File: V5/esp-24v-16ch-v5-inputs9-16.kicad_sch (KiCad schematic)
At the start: 10 parts, among them U11 OR-3H7-4

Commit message: Created V5
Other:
- title: ESP 24V 16xIn/16xOut/4xNTC Module -> ESP 24V 16xIn/16xOut/1-Wire Module
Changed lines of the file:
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@@
 	(paper "A4")
 	(title_block
-		(title "ESP 24V 16xIn/16xOut/4xNTC Module")
-		(date "2025-07-04")
-		(rev "V4.1")
+		(title "ESP 24V 16xIn/16xOut/1-Wire Module")
+		(date "2025-12-09")
+		(rev "V5")
 	)
 	(text "I_{LED} = (24V - V_{LED}) / 6.8k\nI_{LED} = (24V - 2.7V) / 6.8k\nI_{LED} = 3,13 mA"
@@
 		)
 		(instances
-			(project "esp-24v-16ch-v4"
+			(project "esp-24v-16ch-v5"
 				(path "/2bc5a21a-1d79-419d-a592-6852cc07b00a/33bd2dd9-fdba-4639-85e9-44cc18eb8635"
 					(reference "R71")
@@
 		)
 		(instances
-			(project "esp-24v-16ch-v4"
+			(project "esp-24v-16ch-v5"
 				(path "/2bc5a21a-1d79-419d-a592-6852cc07b00a/33bd2dd9-fdba-4639-85e9-44cc18eb8635"
 					(reference "#PWR073")
@@
 		)
 		(instances
-			(project "esp-24v-16ch-v4"
+			(project "esp-24v-16ch-v5"
 				(path "/2bc5a21a-1d79-419d-a592-6852cc07b00a/33bd2dd9-fdba-4639-85e9-44cc18eb8635"
 					(reference "#PWR071")
@@
 		)
 		(instances
-			(project "esp-24v-16ch-v4"
+			(project "esp-24v-16ch-v5"
 				(path "/2bc5a21a-1d79-419d-a592-6852cc07b00a/33bd2dd9-fdba-4639-85e9-44cc18eb8635"
 					(reference "FB11")
@@
 		)
 		(instances
-			(project "esp-24v-16ch-v4"
+			(project "esp-24v-16ch-v5"
 				(path "/2bc5a21a-1d79-419d-a592-6852cc07b00a/33bd2dd9-fdba-4639-85e9-44cc18eb8635"
 					(reference "D39")
@@
 		)
 		(instances
-			(project "esp-24v-16ch-v4"
+			(project "esp-24v-16ch-v5"
 				(path "/2bc5a21a-1d79-419d-a592-6852cc07b00a/33bd2dd9-fdba-4639-85e9-44cc18eb8635"
 					(reference "C51")
@@
 		)
 		(instances
-			(project "esp-24v-16ch-v4"
+			(project "esp-24v-16ch-v5"
 				(path "/2bc5a21a-1d79-419d-a592-6852cc07b00a/33bd2dd9-fdba-4639-85e9-44cc18eb8635"
 					(reference "#PWR075")
@@
 		)
 		(instances
-			(project "esp-24v-16ch-v4"
+			(project "esp-24v-16ch-v5"
 				(path "/2bc5a21a-1d79-419d-a592-6852cc07b00a/33bd2dd9-fdba-4639-85e9-44cc18eb8635"
 					(reference "D40")
@@
 		)
 		(instances
-			(project "esp-24v-16ch-v4"
+			(project "esp-24v-16ch-v5"
 				(path "/2bc5a21a-1d79-419d-a592-6852cc07b00a/33bd2dd9-fdba-4639-85e9-44cc18eb8635"
 					(reference "D41")
@@
 		)
 		(instances
-			(project "esp-24v-16ch-v4"
+			(project "esp-24v-16ch-v5"
 				(path "/2bc5a21a-1d79-419d-a592-6852cc07b00a/33bd2dd9-fdba-4639-85e9-44cc18eb8635"
 					(reference "#PWR077")
@@
 		)
 		(instances
-			(project "esp-24v-16ch-v4"
+			(project "esp-24v-16ch-v5"
 				(path "/2bc5a21a-1d79-419d-a592-6852cc07b00a/33bd2dd9-fdba-4639-85e9-44cc18eb8635"
 					(reference "R72")
@@
 		)
 		(instances
-			(project "esp-24v-16ch-v4"
+			(project "esp-24v-16ch-v5"
 				(path "/2bc5a21a-1d79-419d-a592-6852cc07b00a/33bd2dd9-fdba-4639-85e9-44cc18eb8635"
 					(reference "#PWR074")
@@
 		)
 		(instances
-			(project "esp-24v-16ch-v4"
+			(project "esp-24v-16ch-v5"
 				(path "/2bc5a21a-1d79-419d-a592-6852cc07b00a/33bd2dd9-fdba-4639-85e9-44cc18eb8635"
 					(reference "C50")
@@
 		)
 		(instances
-			(project "esp-24v-16ch-v4"
+			(project "esp-24v-16ch-v5"
 				(path "/2bc5a21a-1d79-419d-a592-6852cc07b00a/33bd2dd9-fdba-4639-85e9-44cc18eb8635"
 					(reference "#PWR076")
@@
 		)
 		(instances
-			(project "esp-24v-16ch-v4"
+			(project "esp-24v-16ch-v5"
 				(path "/2bc5a21a-1d79-419d-a592-6852cc07b00a/33bd2dd9-fdba-4639-85e9-44cc18eb8635"
 					(reference "#PWR072")
@@
 		)
 		(instances
-			(project "esp-24v-16ch-v4"
+			(project "esp-24v-16ch-v5"
 				(path "/2bc5a21a-1d79-419d-a592-6852cc07b00a/33bd2dd9-fdba-4639-85e9-44cc18eb8635"
 					(reference "U11")
@@
 		)
 		(instances
-			(project "esp-24v-16ch-v4"
+			(project "esp-24v-16ch-v5"
 				(path "/2bc5a21a-1d79-419d-a592-6852cc07b00a/33bd2dd9-fdba-4639-85e9-44cc18eb8635"
 					(reference "R70")

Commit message: Updates and corrections to SCH and PCB
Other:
- note added: "I_{LED} = (24V - V_{LED}) / 10k I_{LED} = (24V - 2.7V) / 10k I_{LED} = 2,13 mA"
- note removed: "I_{LED} = (24V - V_{LED}) / 6.8k I_{LED} = (24V - 2.7V) / 6.8k I_{LED} = 3,13 mA"
- moved on the sheet: D34, R64
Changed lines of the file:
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@@
 		(rev "V5")
 	)
-	(text "I_{LED} = (24V - V_{LED}) / 6.8k\nI_{LED} = (24V - 2.7V) / 6.8k\nI_{LED} = 3,13 mA"
+	(text "I_{LED} = (24V - V_{LED}) / 10k\nI_{LED} = (24V - 2.7V) / 10k\nI_{LED} = 2,13 mA"
 		(exclude_from_sim no)
-		(at 106.68 144.78 0)
+		(at 130.81 118.11 0)
 		(effects
 			(font
@@
 	(wire
 		(pts
-			(xy 125.73 116.84) (xy 125.73 120.65)
+			(xy 125.73 121.92) (xy 125.73 125.73)
 		)
 		(stroke
@@
 	(wire
 		(pts
-			(xy 125.73 92.71) (xy 125.73 93.98)
+			(xy 125.73 92.71) (xy 125.73 99.06)
 		)
 		(stroke
@@
 	(wire
 		(pts
-			(xy 125.73 101.6) (xy 125.73 111.76)
+			(xy 125.73 106.68) (xy 125.73 116.84)
 		)
 		(stroke
@@
 	)
 	(label "INLED"
-		(at 125.73 110.49 90)
+		(at 125.73 115.57 90)
 		(effects
 			(font
@@
 	(symbol
 		(lib_id "power:GND")
-		(at 125.73 120.65 0)
+		(at 125.73 125.73 0)
 		(unit 1)
 		(exclude_from_sim no)
@@
 		(dnp no)
 		(property "Reference" "#PWR059"
-			(at 125.73 127 0)
+			(at 125.73 132.08 0)
 			(effects
 				(font
@@
 		)
 		(property "Value" "GND"
-			(at 125.857 125.0442 0)
+			(at 125.857 130.1242 0)
 			(effects
 				(font
@@
 		)
 		(property "Footprint" ""
-			(at 125.73 120.65 0)
+			(at 125.73 125.73 0)
 			(effects
 				(font
@@
 		)
 		(property "Datasheet" ""
-			(at 125.73 120.65 0)
+			(at 125.73 125.73 0)
 			(effects
 				(font
@@
 		)
 		(property "Description" "Power symbol creates a global label with name \"GND\" , ground"
-			(at 125.73 120.65 0)
+			(at 125.73 125.73 0)
 			(effects
 				(font
@@
 	(symbol
 		(lib_id "Device:LED_Small")
-		(at 125.73 114.3 90)
+		(at 125.73 119.38 90)
 		(unit 1)
 		(exclude_from_sim no)
@@
 		(dnp no)
 		(property "Reference" "D34"
-			(at 123.19 113.03 90)
+			(at 123.19 118.11 90)
 			(effects
 				(font
@@
 		)
 		(property "Value" "WHITE/0603"
-			(at 123.19 115.57 90)
+			(at 123.19 120.65 90)
 			(effects
 				(font
@@
 		)
 		(property "Footprint" "Tales:LED_0603_1608Metric"
-			(at 125.73 114.3 90)
+			(at 125.73 119.38 90)
 			(effects
 				(font
@@
 		)
 		(property "Datasheet" "~"
-			(at 125.73 114.3 90)
+			(at 125.73 119.38 90)
 			(effects
 				(font
@@
 		)
 		(property "Description" "Light emitting diode, small symbol"
-			(at 125.73 114.3 0)
+			(at 125.73 119.38 0)
 			(effects
 				(font
@@
 		)
 		(property "Case" "0603/1608"
-			(at 125.73 114.3 0)
+			(at 125.73 119.38 0)
 			(effects
 				(font
@@
 		)
 		(property "Mfr" "Hubei KENTO Elec"
-			(at 125.73 114.3 0)
+			(at 125.73 119.38 0)
 			(effects
 				(font
@@
 		)
 		(property "Mfr PN" "KT-0603W"
-			(at 125.73 114.3 0)
+			(at 125.73 119.38 0)
 			(effects
 				(font
@@
 		)
 		(property "Technology" "~"
-			(at 125.73 114.3 0)
+			(at 125.73 119.38 0)
 			(effects
 				(font
@@
 		)
 		(property "Vendor" "JLCPCB"
-			(at 125.73 114.3 0)
+			(at 125.73 119.38 0)
 			(effects
 				(font
@@
 		)
 		(property "Vendor PN" "C2290"
-			(at 125.73 114.3 0)
+			(at 125.73 119.38 0)
 			(effects
 				(font
@@
 		)
 		(property "LCSC Part #" "C2290"
-			(at 123.19 118.11 90)
+			(at 123.19 123.19 90)
 			(effects
 				(font
@@
 		)
 		(property "JLCPCB BOM" "1"
-			(at 125.73 114.3 0)
+			(at 125.73 119.38 0)
 			(effects
 				(font
@@
 		)
 		(property "Sim.Pin" "1=K 2=A"
-			(at 125.73 114.3 0)
+			(at 125.73 119.38 0)
 			(effects
 				(font
@@
 	(symbol
 		(lib_id "Device:R_US")
-		(at 125.73 97.79 0)
+		(at 125.73 102.87 0)
 		(unit 1)
 		(exclude_from_sim no)
@@
 		(dnp no)
 		(property "Reference" "R64"
-			(at 123.19 95.25 0)
+			(at 123.19 100.33 0)
 			(effects
 				(font
@@
 		)
 		(property "Value" "10k/100mW"
-			(at 123.19 97.79 0)
+			(at 123.19 102.87 0)
 			(effects
 				(font
@@
 		)
 		(property "Footprint" "Tales:R_0603_1608Metric"
-			(at 126.746 98.044 90)
+			(at 126.746 103.124 90)
 			(effects
 				(font
@@
 		)
 		(property "Datasheet" "~"
-			(at 125.73 97.79 0)
+			(at 125.73 102.87 0)
 			(effects
 				(font
@@
 		)
 		(property "Description" "Resistor, US symbol"
-			(at 125.73 97.79 0)
+			(at 125.73 102.87 0)
 			(effects
 				(font
@@
 		)
 		(property "Case" "0603/1608"
-			(at 125.73 97.79 0)
+			(at 125.73 102.87 0)
 			(effects
 				(font
@@
 		)
 		(property "Mfr" "Uniroyal"
-			(at 125.73 97.79 0)
+			(at 125.73 102.87 0)
 			(effects
 				(font
@@
 		)
 		(property "Mfr PN" "0603WAF1002T5E"
-			(at 125.73 97.79 0)
+			(at 125.73 102.87 0)
 			(effects
 				(font
@@
 		)
 		(property "Vendor" "JLCPCB"
-			(at 125.73 97.79 0)
+			(at 125.73 102.87 0)
 			(effects
 				(font
@@
 		)
 		(property "Vendor PN" "C25804"
-			(at 125.73 97.79 0)
+			(at 125.73 102.87 0)
 			(effects
 				(font
@@
 		)
 		(property "Technology" "1%"
-			(at 125.73 97.79 0)
+			(at 125.73 102.87 0)
 			(effects
 				(font
@@
 		)
 		(property "LCSC Part #" "C25804"
-			(at 123.19 100.33 0)
+			(at 123.19 105.41 0)
 			(effects
 				(font
@@
 		)
 		(property "JLCPCB BOM" "1"
-			(at 125.73 97.79 0)
-			(effects
-				(font
+			(at 125.73 102.87 0)
+			(effects
+				(font

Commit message: Many changes!
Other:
- note added: "RESISTORS: 62,5mW WHERE NOT SPECIFIED"
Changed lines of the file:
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@@
+		)
+	)
+	(text "RESISTORS: 62,5mW WHERE NOT SPECIFIED"
+		(exclude_from_sim no)
+		(at 181.61 171.45 0)
+		(effects
+			(font
+				(size 1.905 1.905)
+			)
+			(justify left)
 		)
 	)

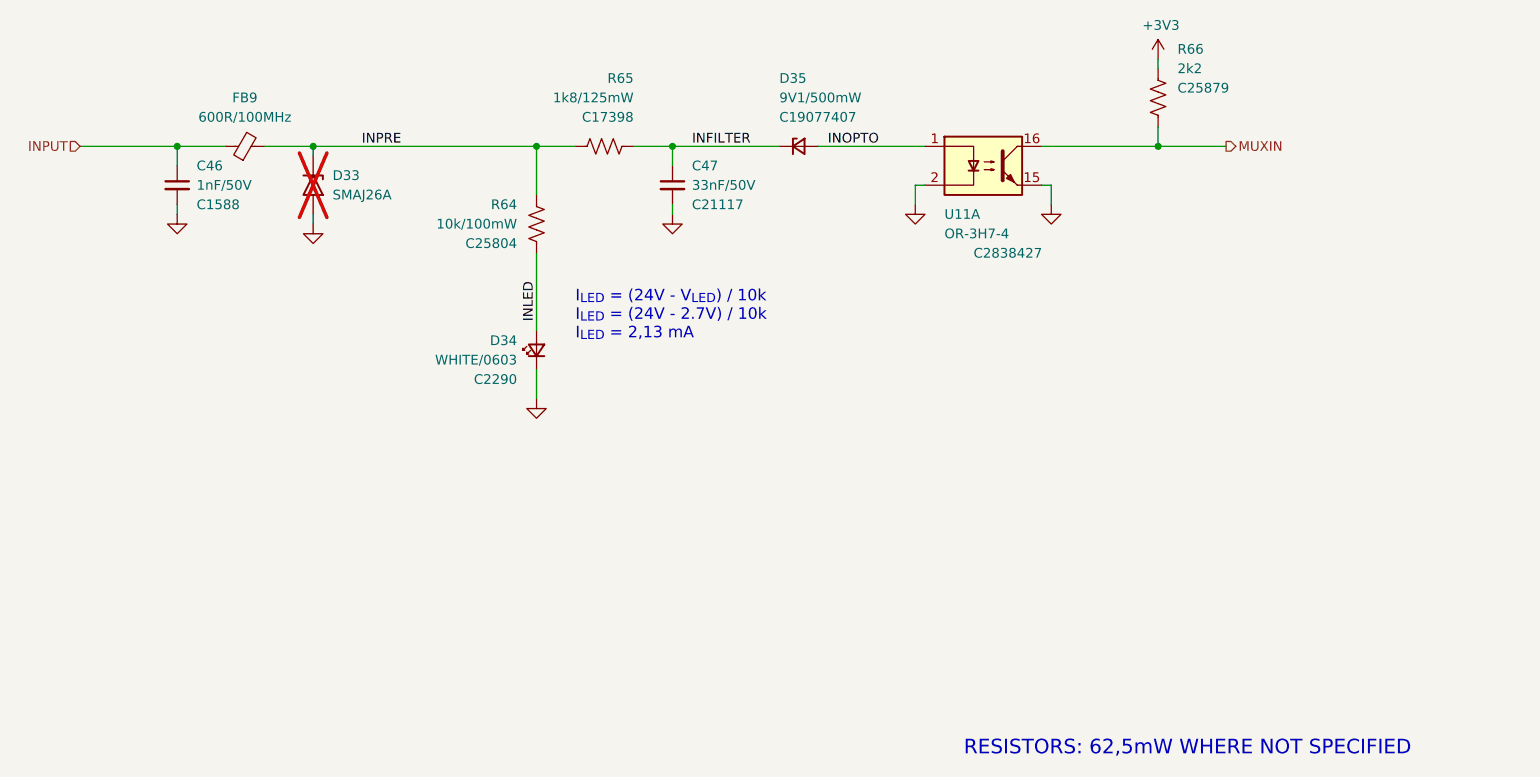
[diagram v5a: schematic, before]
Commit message: Inputs GND separated from main GND.
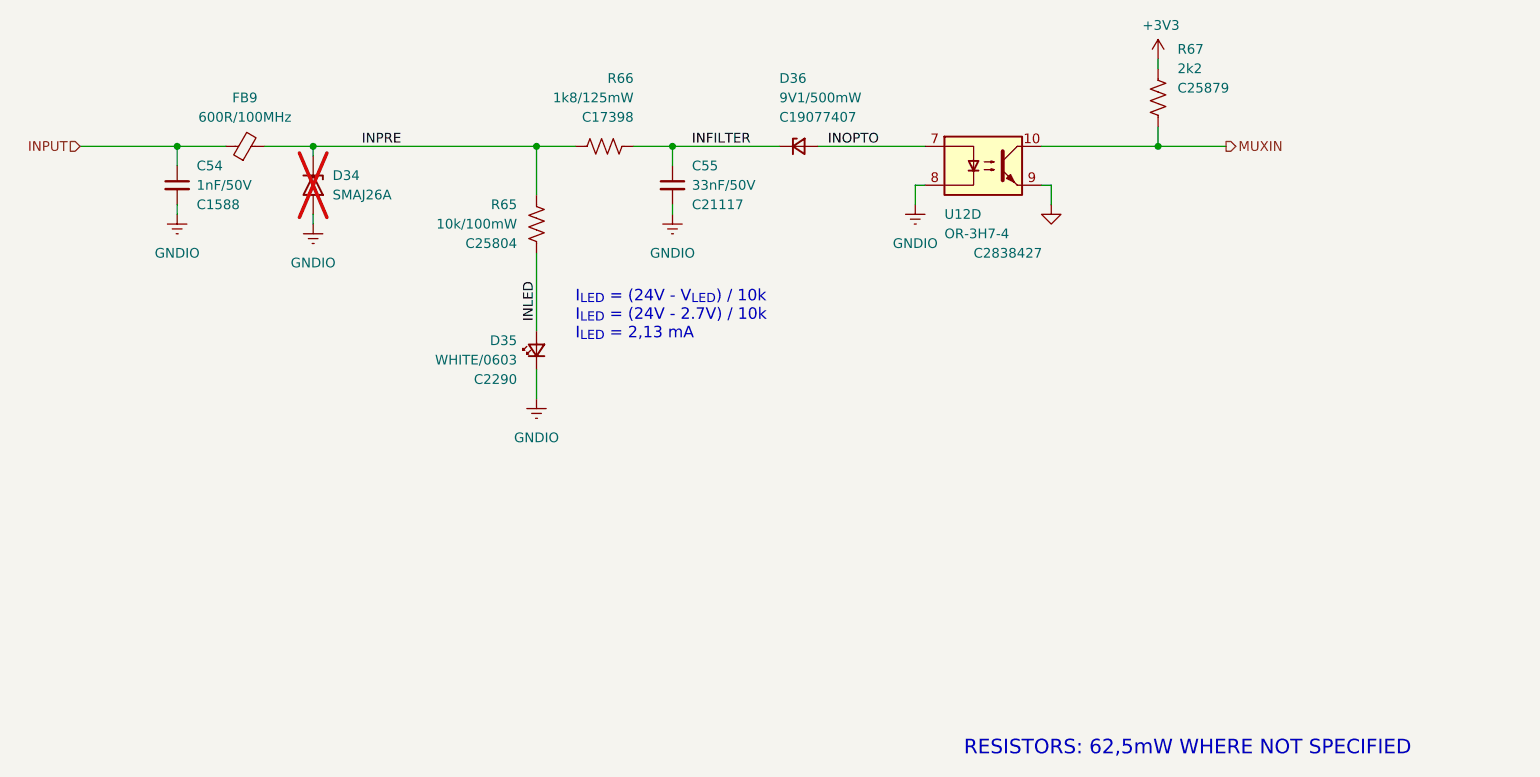
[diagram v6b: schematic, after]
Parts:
- renumbered C46 to C54, C47 to C55, D33 to D34, D34 to D35, D35 to D36, R64 to R65, R65 to R66, R66 to R67, U11 to U12
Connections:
- net GND: now also U12.9; no longer C54.2, C55.2, D34.2 (A2), D35.1 (K), U12.15, U12.2
- net INOPTO: now also U12.7; no longer U12.1
- net MUXIN: now also U12.10; no longer U12.16
- new net GNDIO: C54.2, C55.2, D34.2 (A2), D35.1 (K), U12.8
